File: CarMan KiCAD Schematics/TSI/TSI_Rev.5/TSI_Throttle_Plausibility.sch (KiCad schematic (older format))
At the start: 65 parts, among them Q2 MMBF170, SW1 TS5A3159DBVT, U16 TS372CDT, U18 MCP6004, U22 MCP23016-I_SO, U23 DAC5574IDGS, U3 TS912, U30 TLP293, U6 TS912, U7 MCP6004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

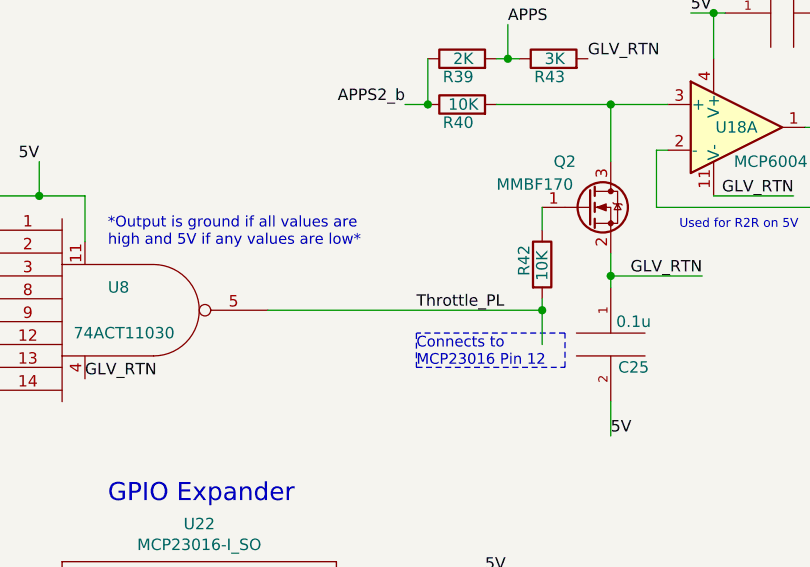
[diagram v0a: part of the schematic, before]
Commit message: Added Comments, added TP for throttle plausiblity
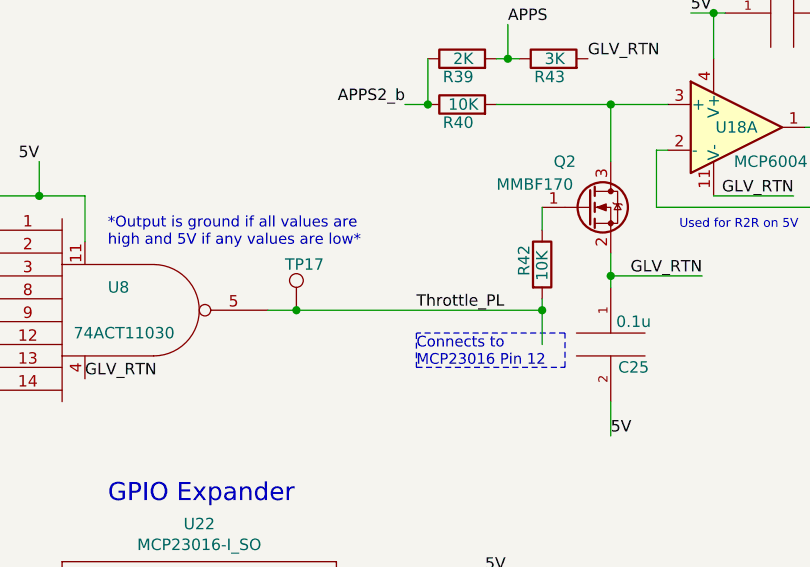
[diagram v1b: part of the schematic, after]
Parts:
- added TP17: Throttle Plaus. TP, symbol Connector:TestPoint
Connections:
- wire segments 295 -> 296
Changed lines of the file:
@@
 NoConn ~ 10250 6700
 Wire Wire Line
-	9750 3700 10950 3700
+	9750 3700 9875 3700
 Wire Wire Line
 	5900 1100 5900 1400
@@
 Text Notes 5000 6850 0    47   ~ 0
 *If the APPS1_ISO and APPS2_b fall \noutside the range of 0.24V-4.76V a \nshort/open is assumed*
+$Comp
+L Connector:TestPoint TP17
+U 1 1 60734148
+P 9875 3700
+F 0 "TP17" H 9825 3900 50  0000 L CNN
+F 1 "Throttle Plaus. TP" H 10000 3850 50  0001 L CNN
+F 2 "" H 10075 3700 50  0001 C CNN
+F 3 "~" H 10075 3700 50  0001 C CNN
+	1    9875 3700
+	1    0    0    -1
+$EndComp
+Connection ~ 9875 3700
+Wire Wire Line
+	9875 3700 10950 3700
 $EndSCHEMATC

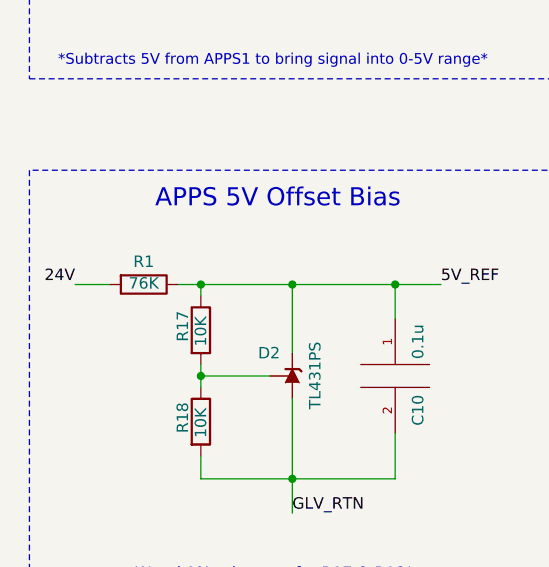
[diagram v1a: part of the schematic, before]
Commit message: Changed R1 from 76K to 1K, fixing the voltage reference (D2) issue for Throttle Plausibility
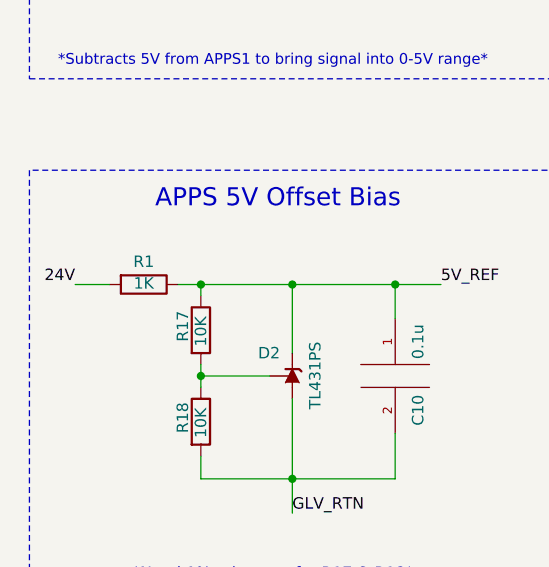
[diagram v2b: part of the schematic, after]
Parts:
- R1: value 76K -> 1K
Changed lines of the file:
@@
 P 1050 6850
 F 0 "R1" V 950 6850 50  0000 C CNN
-F 1 "76K" V 1074 6850 50  0000 C BNN
+F 1 "1K" V 1074 6850 50  0000 C BNN
 F 2 "Resistor_SMD:R_0805_2012Metric_Pad1.15x1.40mm_HandSolder" V 980 6850 50  0001 C CNN
 F 3 "~" H 1050 6850 50  0001 C CNN

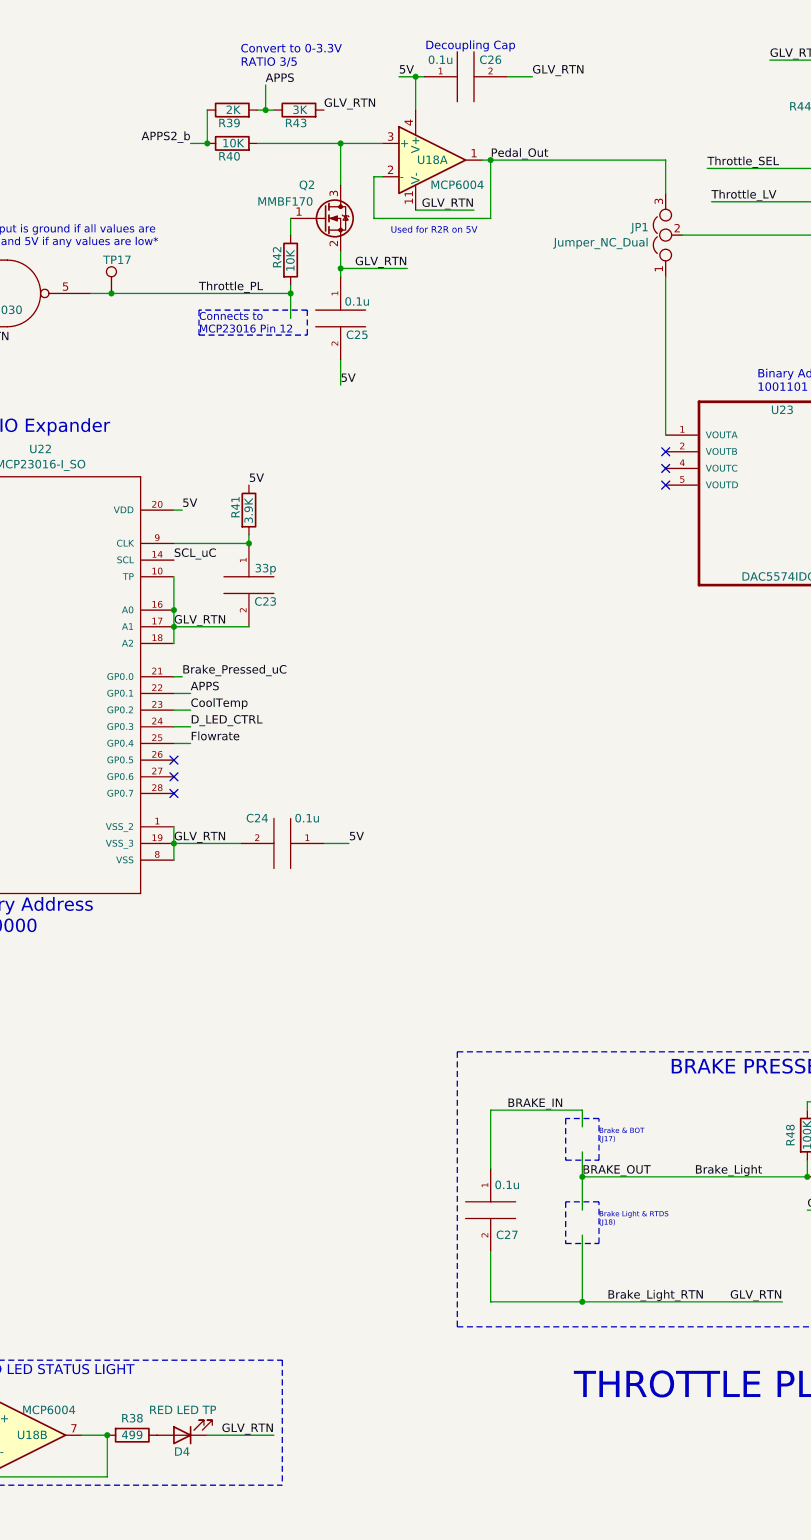
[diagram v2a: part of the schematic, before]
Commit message: - removed testing headers (All pins were easily testable, one that weren't received testing points) - Added pull up resistor at drain of SCADA Relay - Fixed issue with U27-PC_Ready signal not being isolated, also added pull down resistor. Comment about 5V_ISO from logic is necessary - Increased Resistor values across D1 and D4 to cut intensity - Updated PCB board with Netlist
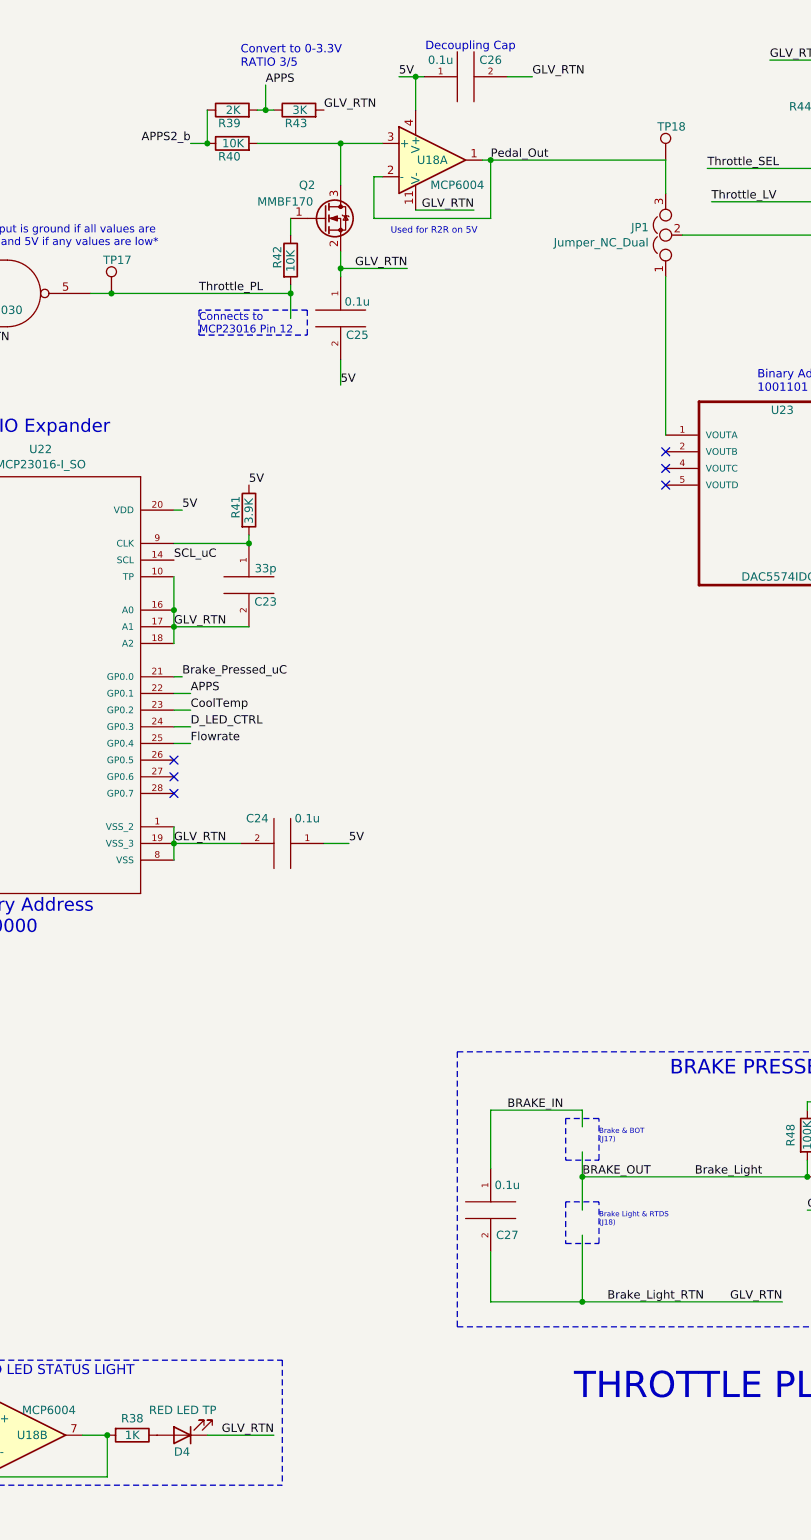
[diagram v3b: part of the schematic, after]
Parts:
- added TP18: Pedal Out, TestPoint:TestPoint_Pad_D3.0mm, symbol Connector:TestPoint
- R38: value 499 -> 1K
- TP17: footprint (none) -> TestPoint:TestPoint_Pad_D3.0mm
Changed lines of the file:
@@
 GLV_RTN
 Connection ~ 9850 10550
-$Comp
-L Device:R R38
-U 1 1 5FE36C1A
-P 10000 10550
-F 0 "R38" V 9900 10550 50  0000 C CNN
-F 1 "499" V 10000 10550 50  0000 C CNN
-F 2 "Resistor_SMD:R_0805_2012Metric_Pad1.15x1.40mm_HandSolder" V 9930 10550 50  0001 C CNN
-F 3 "~" H 10000 10550 50  0001 C CNN
-	1    10000 10550
-	0    1    1    0
-$EndComp
 Text Label 8900 10450 2    50   ~ 0
 Throttle_PL
@@
 F 1 "RED LED TP" H 10500 10400 50  0000 R CNN
 F 2 "LED_SMD:LED_0805_2012Metric_Pad1.15x1.40mm_HandSolder" H 10300 10550 50  0001 C CNN
-F 3 "~" H 10300 10550 50  0001 C CNN
+F 3 "https://www.mouser.com/datasheet/2/678/av02-0112en-ds-hsmx-c1xx-29sep2010-1827222.pdf" H 10300 10550 50  0001 C CNN
 	1    10300 10550
 	-1   0    0    1
@@
 F 0 "TP17" H 9825 3900 50  0000 L CNN
 F 1 "Throttle Plaus. TP" H 10000 3850 50  0001 L CNN
-F 2 "" H 10075 3700 50  0001 C CNN
+F 2 "TestPoint:TestPoint_Pad_D3.0mm" H 10075 3700 50  0001 C CNN
 F 3 "~" H 10075 3700 50  0001 C CNN
 	1    9875 3700
@@
 Wire Wire Line
 	9875 3700 10950 3700
+$Comp
+L Device:R R38
+U 1 1 5FE36C1A
+P 10000 10550
+F 0 "R38" V 9900 10550 50  0000 C CNN
+F 1 "1K" V 10000 10550 50  0000 C CNN
+F 2 "Resistor_SMD:R_0805_2012Metric_Pad1.15x1.40mm_HandSolder" V 9930 10550 50  0001 C CNN
+F 3 "~" H 10000 10550 50  0001 C CNN
+	1    10000 10550
+	0    1    1    0
+$EndComp
+$Comp
+L Connector:TestPoint TP18
+U 1 1 6085F531
+P 13200 2900
+F 0 "TP18" H 13150 3100 50  0000 L CNN
+F 1 "Pedal Out" H 13325 3050 50  0001 L CNN
+F 2 "TestPoint:TestPoint_Pad_D3.0mm" H 13400 2900 50  0001 C CNN
+F 3 "~" H 13400 2900 50  0001 C CNN
+	1    13200 2900
+	1    0    0    -1
+$EndComp
 $EndSCHEMATC

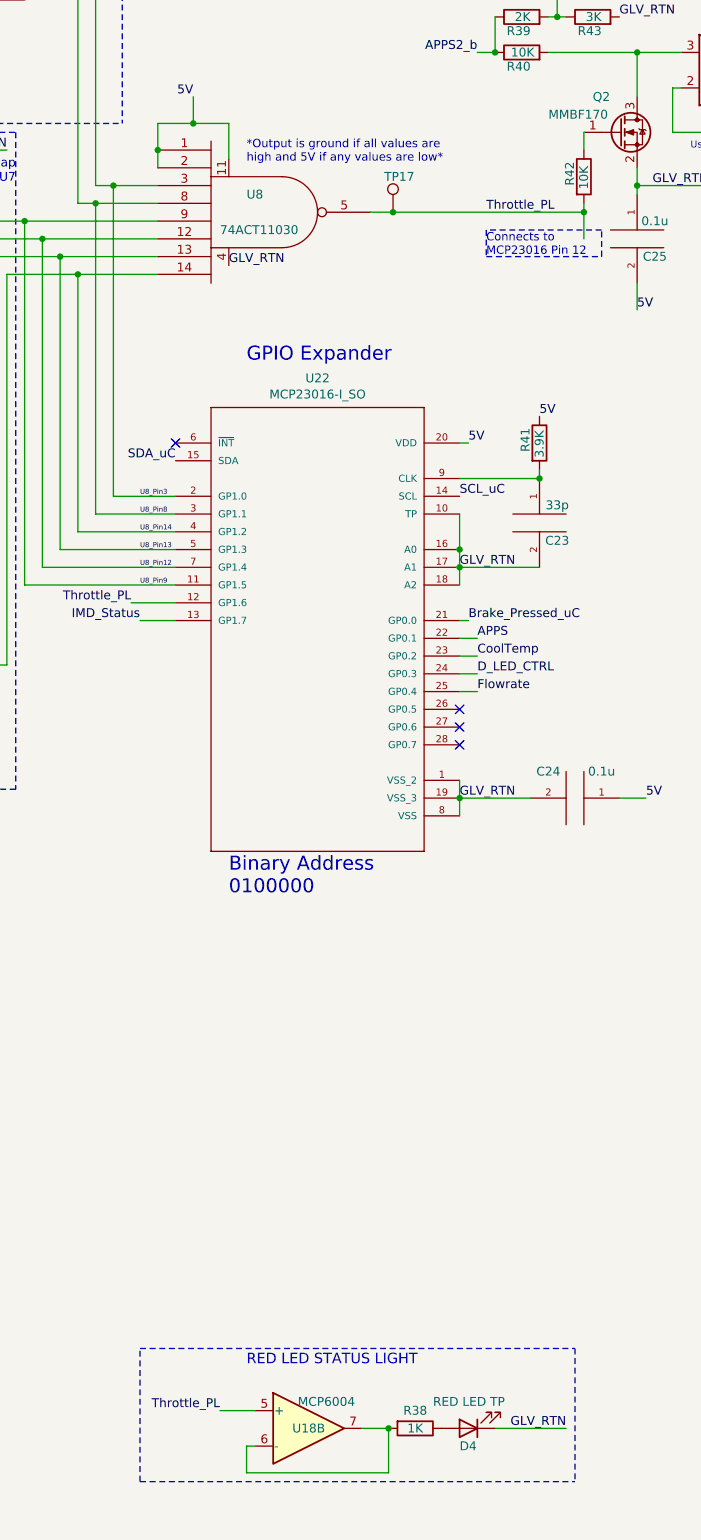
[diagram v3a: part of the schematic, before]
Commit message: - Added a Throttle Plausible Green LED
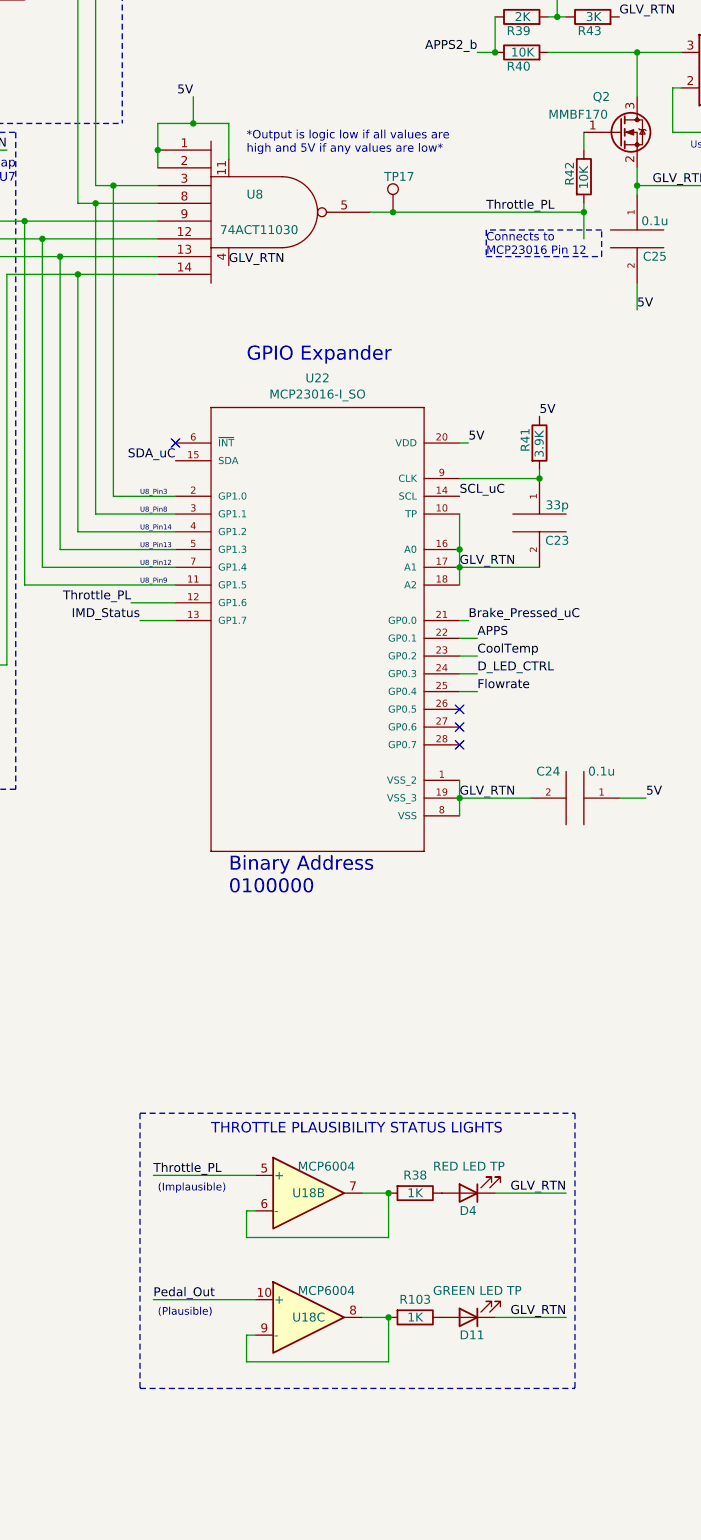
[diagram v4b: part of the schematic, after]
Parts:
- added D11: GREEN LED TP, LED_SMD:LED_0805_2012Metric_Pad1.15x1.40mm_HandSolder, symbol Device:LED
- added R103: 1K, Resistor_SMD:R_0805_2012Metric_Pad1.15x1.40mm_HandSolder, symbol Device:R
- added unit 3 of U18
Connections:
- wire segments 296 -> 303
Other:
- note added: "(Implausible)"
- note added: "(Plausible)"
- note added: "*Output is logic low if all values are \nhigh and 5V if any values are low*"
- note added: "THROTTLE PLAUSIBILITY STATUS LIGHTS"
- note removed: "*Output is ground if all values are \nhigh and 5V if any values are low*"
- note removed: "RED LED STATUS LIGHT"
- moved on the sheet: D4, R38, U18B
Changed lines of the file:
@@
 Wire Wire Line
 	12150 8600 12700 8600
-Wire Notes Line
-	8450 10850 8450 10100
 Text Notes 13225 8400 0    87   ~ 0
 BRAKE PRESSED
-Text Notes 9050 10200 0    59   ~ 0
-RED LED STATUS LIGHT
-Text Label 10850 10550 2    50   ~ 0
-GLV_RTN
-Connection ~ 9850 10550
-Text Label 8900 10450 2    50   ~ 0
+Text Notes 8850 8900 0    59   ~ 0
+THROTTLE PLAUSIBILITY STATUS LIGHTS
+Text Label 10850 9225 2    50   ~ 0
+GLV_RTN
+Connection ~ 9850 9225
+Text Label 8525 9125 0    50   ~ 0
 Throttle_PL
 Wire Wire Line
-	9050 10650 9100 10650
-Wire Wire Line
-	9850 10550 9700 10550
-Wire Wire Line
-	9850 10800 9850 10550
-Wire Wire Line
-	9050 10800 9850 10800
-Wire Wire Line
-	9050 10650 9050 10800
-Wire Wire Line
-	8900 10450 9100 10450
+	9050 9325 9100 9325
+Wire Wire Line
+	9850 9225 9700 9225
+Wire Wire Line
+	9850 9475 9850 9225
+Wire Wire Line
+	9050 9475 9850 9475
+Wire Wire Line
+	9050 9325 9050 9475
 Text HLabel 1550 2200 0    50   Input ~ 0
 BRAKE_IN(AIRS+)
@@
 GLV_RTN
 Wire Notes Line
-	8450 10100 10900 10100
-Wire Notes Line
-	8450 10850 10900 10850
-Wire Notes Line
-	10900 10100 10900 10850
+	8450 8775 10900 8775
 Wire Wire Line
 	10250 7000 10650 7000
@@
 L Amplifier_Operational:MCP6004 U18
 U 2 1 5FB98A0D
-P 9400 10550
-F 0 "U18" H 9400 10550 50  0000 C CNN
-F 1 "MCP6004" H 9500 10700 50  0000 C CNN
-F 2 "TSI_Rev_2021_Footprint_Lib:SOIC127P600X175-14N" H 9350 10650 50  0001 C CNN
-F 3 "http://ww1.microchip.com/downloads/en/DeviceDoc/21733j.pdf" H 9450 10750 50  0001 C CNN
-	2    9400 10550
+P 9400 9225
+F 0 "U18" H 9400 9225 50  0000 C CNN
+F 1 "MCP6004" H 9500 9375 50  0000 C CNN
+F 2 "TSI_Rev_2021_Footprint_Lib:SOIC127P600X175-14N" H 9350 9325 50  0001 C CNN
+F 3 "http://ww1.microchip.com/downloads/en/DeviceDoc/21733j.pdf" H 9450 9425 50  0001 C CNN
+	2    9400 9225
 	1    0    0    -1
 $EndComp
@@
 L Device:LED D?
 U 1 1 60834B36
-P 10300 10550
+P 10300 9225
 AR Path="/5FE1DCBA/60834B36" Ref="D?"  Part="1"
 AR Path="/5FC85F57/60834B36" Ref="D4"  Part="1"
-F 0 "D4" H 10350 10650 50  0000 R CNN
-F 1 "RED LED TP" H 10500 10400 50  0000 R CNN
-F 2 "LED_SMD:LED_0805_2012Metric_Pad1.15x1.40mm_HandSolder" H 10300 10550 50  0001 C CNN
-F 3 "https://www.mouser.com/datasheet/2/678/av02-0112en-ds-hsmx-c1xx-29sep2010-1827222.pdf" H 10300 10550 50  0001 C CNN
-	1    10300 10550
+F 0 "D4" H 10350 9325 50  0000 R CNN
+F 1 "RED LED TP" H 10500 9075 50  0000 R CNN
+F 2 "LED_SMD:LED_0805_2012Metric_Pad1.15x1.40mm_HandSolder" H 10300 9225 50  0001 C CNN
+F 3 "https://www.mouser.com/datasheet/2/678/av02-0112en-ds-hsmx-c1xx-29sep2010-1827222.pdf" H 10300 9225 50  0001 C CNN
+	1    10300 9225
 	-1   0    0    1
 $EndComp
 Wire Wire Line
-	10450 10550 10850 10550
+	10450 9225 10850 9225
 Text Notes 600  10350 0    31   ~ 0
 Throttle Plausibility\nConnects to pedals:\nAPPS1 2K POT
@@
 	1    0    0    -1
 $EndComp
-Text Notes 9050 3425 0    47   ~ 0
-*Output is ground if all values are \nhigh and 5V if any values are low*
+Text Notes 9050 3375 0    47   ~ 0
+*Output is logic low if all values are \nhigh and 5V if any values are low*
 Text Notes 5000 6850 0    47   ~ 0
 *If the APPS1_ISO and APPS2_b fall \noutside the range of 0.24V-4.76V a \nshort/open is assumed*
@@
 L Device:R R38
 U 1 1 5FE36C1A
-P 10000 10550
-F 0 "R38" V 9900 10550 50  0000 C CNN
-F 1 "1K" V 10000 10550 50  0000 C CNN
-F 2 "Resistor_SMD:R_0805_2012Metric_Pad1.15x1.40mm_HandSolder" V 9930 10550 50  0001 C CNN
-F 3 "~" H 10000 10550 50  0001 C CNN
-	1    10000 10550
+P 10000 9225
+F 0 "R38" V 9900 9225 50  0000 C CNN
+F 1 "1K" V 10000 9225 50  0000 C CNN
+F 2 "Resistor_SMD:R_0805_2012Metric_Pad1.15x1.40mm_HandSolder" V 9930 9225 50  0001 C CNN
+F 3 "~" H 10000 9225 50  0001 C CNN
+	1    10000 9225
 	0    1    1    0
 $EndComp
@@
 	1    0    0    -1
 $EndComp
+Text Label 10850 9925 2    50   ~ 0
+GLV_RTN
+Connection ~ 9850 9925
+Wire Wire Line
+	9050 10025 9100 10025
+Wire Wire Line
+	9850 9925 9700 9925
+Wire Wire Line
+	9850 10175 9850 9925
+Wire Wire Line
+	9050 10175 9850 10175
+Wire Wire Line
+	9050 10025 9050 10175
+$Comp
+L Amplifier_Operational:MCP6004 U18
+U 3 1 60823F76
+P 9400 9925
+F 0 "U18" H 9400 9925 50  0000 C CNN
+F 1 "MCP6004" H 9500 10075 50  0000 C CNN
+F 2 "TSI_Rev_2021_Footprint_Lib:SOIC127P600X175-14N" H 9350 10025 50  0001 C CNN
+F 3 "http://ww1.microchip.com/downloads/en/DeviceDoc/21733j.pdf" H 9450 10125 50  0001 C CNN
+	3    9400 9925
+	1    0    0    -1
+$EndComp
+$Comp
+L Device:LED D?
+U 1 1 60823F7C
+P 10300 9925
+AR Path="/5FE1DCBA/60823F7C" Ref="D?"  Part="1"
+AR Path="/5FC85F57/60823F7C" Ref="D11"  Part="1"
+F 0 "D11" H 10350 10025 50  0000 R CNN
+F 1 "GREEN LED TP" H 10500 9775 50  0000 R CNN
+F 2 "LED_SMD:LED_0805_2012Metric_Pad1.15x1.40mm_HandSolder" H 10300 9925 50  0001 C CNN
+F 3 "https://www.mouser.com/datasheet/2/678/av02-0112en-ds-hsmx-c1xx-29sep2010-1827222.pdf" H 10300 9925 50  0001 C CNN
+	1    10300 9925
+	-1   0    0    1
+$EndComp
+Wire Wire Line
+	10450 9925 10850 9925
+$Comp
+L Device:R R103
+U 1 1 60823F83
+P 10000 9925
+F 0 "R103" V 9900 9925 50  0000 C CNN
+F 1 "1K" V 10000 9925 50  0000 C CNN
+F 2 "Resistor_SMD:R_0805_2012Metric_Pad1.15x1.40mm_HandSolder" V 9930 9925 50  0001 C CNN
+F 3 "~" H 10000 9925 50  0001 C CNN
+	1    10000 9925
+	0    1    1    0
+$EndComp
+Wire Notes Line
+	10900 8775 10900 10325
+Wire Notes Line
+	8450 8775 8450 10325
+Wire Notes Line
+	8450 10325 10900 10325
+Text Label 8525 9825 0    50   ~ 0
+Pedal_Out
+Wire Wire Line
+	8525 9825 9100 9825
+Wire Wire Line
+	8525 9125 9100 9125
+Text Notes 8550 9925 0    43   ~ 0
+(Plausible)
+Text Notes 8550 9225 0    43   ~ 0
+(Implausible)
 $EndSCHEMATC
